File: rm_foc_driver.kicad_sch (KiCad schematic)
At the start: 69 parts, among them J1 SWD, J2 SENSOR, J3 UART, J4 TMC4671, J5 PWM, J6 Conn_01x02, J7 CURRENT_SENSE, J8 Conn_01x03, Q1 IRF7580M, Q2 IRF7580M, Q3 IRF7580M, Q4 IRF7580M, Q5 IRF7580M, Q6 IRF7580M, U1 TPS54540, U2 RT9013, U3 STM32F401CCUx, U4 DRV8303, U5 AS5047D, Y1 Crystal_GND24

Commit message: Not complete yet
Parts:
- removed C1: 10uF, Capacitor_SMD:C_0603_1608Metric, symbol Device:C
- removed C14, C18, C19, C20: 100nF, Capacitor_SMD:C_0603_1608Metric, symbol Device:C
- removed C17: 1uF, Capacitor_SMD:C_0603_1608Metric, symbol Device:C
- removed C21: 2.2nF, Capacitor_SMD:C_0603_1608Metric, symbol Device:C
- removed J7: CURRENT_SENSE, Connector_PinHeader_2.54mm:PinHeader_1x02_P2.54mm_Vertical, symbol Connector_Generic:Conn_01x02
- removed U4: DRV8303, Package_SO:TSSOP-48_6.1x12.5mm_P0.5mm, symbol Driver_Motor:DRV8303
- removed U5: AS5047D, Package_SO:TSSOP-14_4.4x5mm_P0.65mm, symbol Sensor_Magnetic:AS5047D
- added C10: 100nF, Capacitor_SMD:C_0603_1608Metric, symbol Device:C
- added D4, D5, D6: DIODE, Diode_SMD:D_SMA, symbol pspice:DIODE
- added R12: 200k, Resistor_SMD:R_0603_1608Metric, symbol Device:R
- added R13, R14, R15, R16, R17, R18: 10R, Resistor_SMD:R_0603_1608Metric, symbol Device:R
- added U4: EG2133, Package_SO:TSSOP-20_4.4x6.5mm_P0.65mm, symbol Driver_FET:EG2133
- added U6: INA2180, Package_SO:VSSOP-8_3.0x3.0mm_P0.65mm, symbol Amplifier_Current:INA2180
- added U7: MT6701, Package_SO:SOP-8_3.9x4.9mm_P1.27mm, symbol Sensor_Magnetic:MT6701
- C12, C13: value 1uF -> 100nF
- C15: value 2.2uF -> 1uF
- C16: value 4.7uF -> 1uF; footprint Capacitor_SMD:C_0805_2012Metric -> Capacitor_SMD:C_0603_1608Metric
- R9: value 1R -> 200k
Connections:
- net +12V: no longer C16.1
- net +5V: now also C15.1, C16.1, R9.1, D4.1 (K), D5.1 (K), D6.1 (K), R12.2, U4.7 (VCC), U6.8 (VS), U7.1 (VDD)
- net GH_A: now also R13.2
- net GH_B: now also R15.2
- net GH_C: now also R17.2
- net GL_A: now also R14.2
- net GL_B: now also R16.2
- net GL_C: now also R18.2
- net GND: now also C15.2, U4.8 (GND), U6.2 (IN1-), U6.4 (GND), U6.6 (IN2-), U7.4 (GND); no longer C12.2, C13.2, C15.1, R9.2
- net PWM1: now also U4.1 (HIN1)
- net PWM2: now also U4.2 (HIN2)
- net PWM3: now also U4.3 (HIN3)
- net PWM4: now also U4.4 (~{LIN1})
- net PWM5: now also U4.5 (~{LIN2})
- net PWM6: now also U4.6 (~{LIN3})
- net SH_A: now also C10.2, U4.12 (VS1)
- net SH_B: now also C12.2, U4.15 (VS2)
- net SH_C: now also C13.2, U4.18 (VS3)
- net SL_A: now also U6.3 (IN1+)
- net SL_B: now also U6.5 (IN2+)
- net SO1: now also U6.1 (OUT1)
- net SO2: now also U6.7 (OUT2)
- net at C12.1: now also D5.2 (A), U4.17 (VB2)
- net at C13.1: now also D4.2 (A), U4.20 (VB3)
- new net: R14.1, U4.9 (LO1)
- new net: R13.1, U4.13 (HO1)
- new net: R16.1, U4.10 (LO2)
- new net: R18.1, U4.11 (LO3)
- new net: C10.1, D6.2 (A), U4.14 (VB1)
- new net: R15.1, U4.16 (HO2)
- new net: R17.1, U4.19 (HO3)
- new net: R9.2, U7.2 (MODE)
- new net: R12.1, U7.8 (Z)
- no-connect marks 30 -> 25

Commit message: new verson of pcb.ready to print
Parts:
- removed J2: SENSOR, Connector_PinHeader_2.54mm:PinHeader_1x03_P2.54mm_Vertical, symbol Connector_Generic:Conn_01x03
- removed R12, R9: 200k, Resistor_SMD:R_0603_1608Metric, symbol Device:R
- D3, D4, D5, D6: footprint Diode_SMD:D_SMA -> Diode_SMD:D_SOD-123
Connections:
- net CS1: now also U7.8 (Z)
- net CS2: now also J4.4 (Pin_4)
- net MISO: now also U7.6 (A)
- net OSC_IN: now also C9.1, Y1.1; no longer C11.1, Y1.3
- net OSC_OUT: now also C11.1, Y1.3; no longer C9.1, Y1.1
- net SCLK: now also U7.7 (B)
- net ADC1: now reaches U3.18 (PB0)
- net ADC1: now also U7.3 (OUT)
- net MODE: now reaches U3.19 (PB1)
- net MODE: now also U7.2 (MODE)
- net CS3: no longer names the net of U3.29 (PA8)
- net CS3: no longer J4.4 (Pin_4)
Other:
- moved on the sheet: C16, J8, U7

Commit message: Update pcb-layout.Not complete yet.Current progress 50%.
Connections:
- net DC_CAL: no longer names the net of U3.11 (PA1)
- net EN_GATE: no longer names the net of U3.12 (PA2)
- no-connect marks 25 -> 27
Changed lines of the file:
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@@
   (junction (at 217.805 232.41) (diameter 0) (color 0 0 0 0)
   )
+  (no_connect (at 113.665 252.095))
+  (no_connect (at 113.665 254.635))
   (no_connect (at 113.665 249.555))
   (no_connect (at 69.85 46.99))
@@
     (stroke (width 0) (type default) (color 0 0 0 0))
   )
-  (wire (pts (xy 113.665 254.635) (xy 123.825 254.635))
-    (stroke (width 0) (type default) (color 0 0 0 0))
-  )
   (wire (pts (xy 71.755 267.335) (xy 80.645 267.335))
     (stroke (width 0) (type default) (color 0 0 0 0))
@@
   )
   (wire (pts (xy 30.48 340.36) (xy 43.815 340.36))
-    (stroke (width 0) (type default) (color 0 0 0 0))
-  )
-  (wire (pts (xy 113.665 252.095) (xy 123.825 252.095))
     (stroke (width 0) (type default) (color 0 0 0 0))
   )
@@
     (effects (font (size 1.27 1.27)) (justify left bottom))
   )
-  (label "EN_GATE" (at 123.825 254.635 0)
-    (effects (font (size 1.27 1.27)) (justify left bottom))
-  )
   (label "CS2" (at 123.825 259.715 0)
     (effects (font (size 1.27 1.27)) (justify left bottom))
@@
     (effects (font (size 1.27 1.27)) (justify left bottom))
   )
-  (label "DC_CAL" (at 123.825 252.095 0)
-    (effects (font (size 1.27 1.27)) (justify left bottom))
-  )

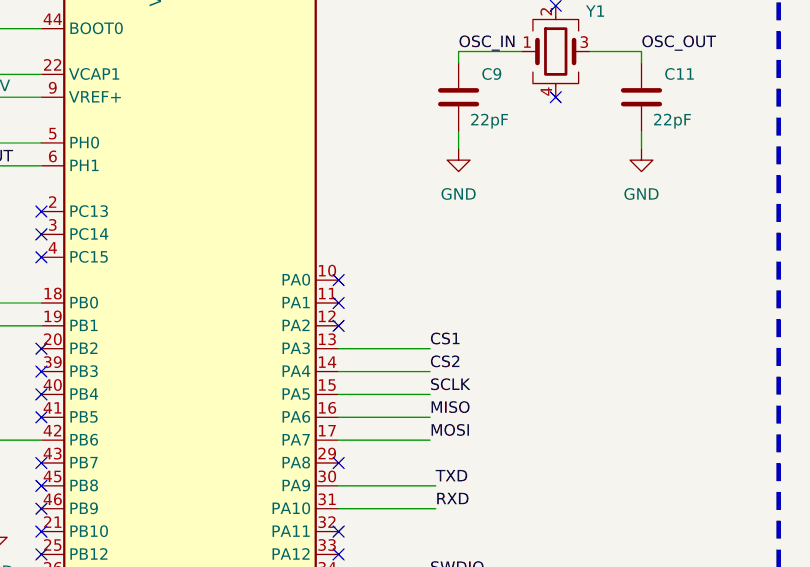
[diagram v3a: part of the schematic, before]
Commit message: Straight line version.
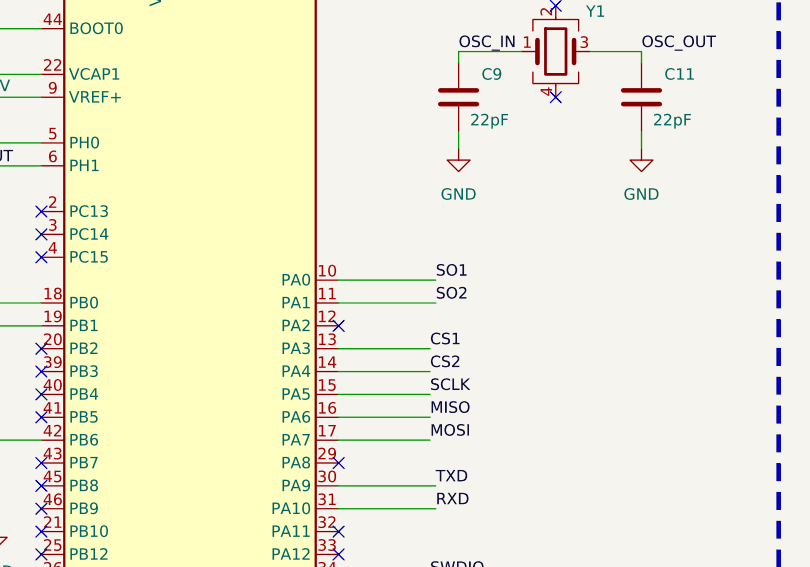
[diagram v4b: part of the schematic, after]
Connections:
- net SO1: now also U3.10 (PA0)
- net SO2: now also U3.11 (PA1)
- no-connect marks 27 -> 25
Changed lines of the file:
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@@
   (junction (at 217.805 232.41) (diameter 0) (color 0 0 0 0)
   )
-  (no_connect (at 113.665 252.095))
   (no_connect (at 113.665 254.635))
-  (no_connect (at 113.665 249.555))
   (no_connect (at 69.85 46.99))
   (no_connect (at 137.795 229.235))
@@
     (stroke (width 0) (type default) (color 0 0 0 0))
   )
+  (wire (pts (xy 113.665 249.555) (xy 124.46 249.555))
+    (stroke (width 0) (type default) (color 0 0 0 0))
+  )
   (wire (pts (xy 113.665 267.335) (xy 123.825 267.335))
     (stroke (width 0) (type default) (color 0 0 0 0))
@@
   )
   (wire (pts (xy 71.755 274.32) (xy 75.565 274.32))
+    (stroke (width 0) (type default) (color 0 0 0 0))
+  )
+  (wire (pts (xy 113.665 252.095) (xy 124.46 252.095))
     (stroke (width 0) (type default) (color 0 0 0 0))
   )
@@
     (effects (font (size 1.27 1.27)) (justify left bottom))
   )
+  (label "SO1" (at 124.46 249.555 0)
+    (effects (font (size 1.27 1.27)) (justify left bottom))
+  )
   (label "SCLK" (at 90.17 342.9 0)
     (effects (font (size 1.27 1.27)) (justify left bottom))
@@
     (effects (font (size 1.27 1.27)) (justify left bottom))
   )
+  (label "SO2" (at 124.46 252.095 0)
+    (effects (font (size 1.27 1.27)) (justify left bottom))
+  )

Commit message: Fcuk IRF7580 fuck fuck.csd18540 is better
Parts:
- removed J5: PWM, Connector_PinHeader_2.54mm:PinHeader_1x06_P2.54mm_Vertical, symbol Connector_Generic:Conn_01x06
- removed Q1, Q2, Q3, Q4, Q5, Q6: IRF7580M, Package_DirectFET:DirectFET_ME, symbol Transistor_FET:IRF7580M
- added J5: Conn_01x07, Connector_PinHeader_2.54mm:PinHeader_1x07_P2.54mm_Vertical, symbol Connector_Generic:Conn_01x07
- added Q1, Q2, Q3, Q4, Q5, Q6: CSD18540Q5B, Package_TO_SOT_SMD:TDSON-8-1, symbol Transistor_FET:CSD18540Q5B
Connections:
- net +12V: now also Q1.5 (D), Q3.5 (D), Q5.5 (D)
- net GH_A: now also Q1.4 (G)
- net GH_B: now also Q3.4 (G)
- net GH_C: now also Q5.4 (G)
- net GL_A: now also Q2.4 (G)
- net GL_B: now also Q4.4 (G)
- net GL_C: now also Q6.4 (G)
- net GND: now also J5.7 (Pin_7), Q6.1 (S), Q6.2 (S), Q6.3 (S)
- net PWM1: now also J5.1 (Pin_1)
- net PWM2: now also J5.2 (Pin_2)
- net PWM3: now also J5.3 (Pin_3)
- net PWM4: now also J5.4 (Pin_4)
- net PWM5: now also J5.5 (Pin_5)
- net PWM6: now also J5.6 (Pin_6)
- net SH_A: now also Q1.1 (S), Q1.2 (S), Q1.3 (S), Q2.5 (D)
- net SH_B: now also Q3.1 (S), Q3.2 (S), Q3.3 (S), Q4.5 (D)
- net SH_C: now also Q5.1 (S), Q5.2 (S), Q5.3 (S), Q6.5 (D)
- net SL_A: now also Q2.1 (S), Q2.2 (S), Q2.3 (S)
- net SL_B: now also Q4.1 (S), Q4.2 (S), Q4.3 (S)

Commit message: ir2104 version
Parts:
- removed J5: Conn_01x07, Connector_PinHeader_2.54mm:PinHeader_1x07_P2.54mm_Vertical, symbol Connector_Generic:Conn_01x07
- removed R17, R18: 10R, Resistor_SMD:R_0603_1608Metric, symbol Device:R
- removed U4: EG2133, Package_SO:TSSOP-20_4.4x6.5mm_P0.65mm, symbol Driver_FET:EG2133
- added C1: 1uF, Capacitor_SMD:C_0603_1608Metric, symbol Device:C
- added C14, C17, C18: 100nF, Capacitor_SMD:C_0603_1608Metric, symbol Device:C
- added J2: TMC4671, Connector_PinHeader_2.54mm:PinHeader_1x04_P2.54mm_Vertical, symbol Connector_Generic:Conn_01x04
- added R12, R9: 20R, Resistor_SMD:R_0603_1608Metric, symbol Device:R
- added U10: 74HC244, Package_SO:TSSOP-20_4.4x5mm_P0.5mm, symbol 74xx:74HC244
- added U4: AMS1117-5.0, Package_TO_SOT_SMD:SOT-223-3_TabPin2, symbol Regulator_Linear:AMS1117-5.0
- added U5, U8, U9: IR2104, Package_SO:SOIC-8W_5.3x5.3mm_P1.27mm, symbol Driver_FET:IR2104
- R13, R14, R15, R16: value 10R -> 20R
- R7: value 105k -> 210k
- R8: value 20k -> 15k
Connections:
- net +12V: now also C10.1, C12.1, C13.1, D4.1 (K), D5.1 (K), D6.1 (K), L1.2, R7.1, C1.1, U4.3 (VI), U5.1 (VCC), U5.3 (~{SD}), U8.1 (VCC), U8.3 (~{SD}), U9.1 (VCC), U9.3 (~{SD}); no longer C22.1, C24.1, C25.1, C26.1, C27.1, C29.1, C3.1, C30.1, C31.1, C32.1, C33.1, J6.2 (Pin_2), Q1.5 (D), Q3.5 (D), Q5.5 (D), U1.2 (VIN)
- net +5V: now also U10.20 (VCC), U4.2 (VO); no longer D4.1 (K), D5.1 (K), D6.1 (K), L1.2, R7.1
- net GH_A: now also R13.1; no longer R13.2
- net GH_B: now also R9.1; no longer R15.2
- net GH_C: now also R15.1
- net GL_A: now also R14.1; no longer R14.2
- net GL_B: now also R12.1; no longer R16.2
- net GL_C: now also R16.1
- net GND: now also C10.2, C12.2, C13.2, C1.2, J2.4 (Pin_4), U10.1 (1OE), U10.10 (GND), U4.1 (GND), U5.4 (COM), U8.4 (COM), U9.4 (COM)
- net PWM1: now also J2.1 (Pin_1), U10.2 (1A0)
- net PWM2: now also J2.2 (Pin_2), U10.4 (1A1)
- net PWM3: now also J2.3 (Pin_3), U10.6 (1A2)
- net SH_A: now also C17.2, U8.6 (VS); no longer C10.2
- net SH_B: now also C14.2, U5.6 (VS); no longer C12.2
- net SH_C: now also C18.2, U9.6 (VS); no longer C13.2
- net at D4.2 (A): now also C14.1, U5.8 (VB); no longer C13.1
- net at D5.2 (A): now also C17.1, U8.8 (VB); no longer C12.1
- net at D6.2 (A): now also C18.1, U9.8 (VB); no longer C10.1
- new net: R16.2, U9.5 (LO)
- new net: R15.2, U9.7 (HO)
- new net: R14.2, U8.5 (LO)
- new net: R13.2, U8.7 (HO)
- new net: R12.2, U5.5 (LO)
- new net: R9.2, U5.7 (HO)
- new net +24V: C22.1, C24.1, C25.1, C26.1, C27.1, C29.1, C3.1, C30.1, C31.1, C32.1, C33.1, J6.2 (Pin_2), Q1.5 (D), Q3.5 (D), Q5.5 (D), U1.2 (VIN)
- new net PWMA: U10.18 (1Y0), U9.2 (IN)
- new net PWMB: U10.16 (1Y1), U5.2 (IN)
- new net PWMC: U10.14 (1Y2), U8.2 (IN)
- no-connect marks 25 -> 36
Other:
- note added: "BUCK TO 12V"
- note added: "CURRENT SENSE"
- note added: "Chen Yulong"
- note added: "DynamicX"
- note added: "ISOLATE"
- note added: "POSITION SENSOR"
- note removed: "SENSOR"
- company: (none) -> Chen Yulong
- title: (none) -> DynamicX FOC_Driver
- moved on the sheet: C11, C15, C2, C22, C24, C25, C26, C27, C29, C30, C31, C32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

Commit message: update package
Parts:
- U10: footprint Package_SO:TSSOP-20_4.4x5mm_P0.5mm -> Package_SO:TSSOP-20_4.4x6.5mm_P0.65mm
- U5, U8, U9: footprint Package_SO:SOIC-8W_5.3x5.3mm_P1.27mm -> Package_SO:SOP-8_3.9x4.9mm_P1.27mm
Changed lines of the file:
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@@
     (stroke (width 0) (type default) (color 0 0 0 0))
   )
-  (wire (pts (xy 193.04 281.94) (xy 193.04 297.18))
+  (wire (pts (xy 193.04 281.94) (xy 193.04 290.195))
     (stroke (width 0) (type default) (color 0 0 0 0))
   )
@@
       (effects (font (size 1.27 1.27)) (justify left))
     )
-    (property "Footprint" "Package_SO:SOIC-8W_5.3x5.3mm_P1.27mm" (id 2) (at 213.36 57.15 0)
-      (effects (font (size 1.27 1.27) italic) hide)
+    (property "Footprint" "Package_SO:SOP-8_3.9x4.9mm_P1.27mm" (id 2) (at 213.36 57.15 0)
+      (effects (font (size 1.27 1.27) italic))
     )
     (property "Datasheet" "https://www.infineon.com/dgdl/ir2104.pdf?fileId=5546d462533600a4015355c7c1c31671" (id 3) (at 213.36 57.15 0)
@@
       (effects (font (size 1.27 1.27)) (justify left))
     )
-    (property "Footprint" "Package_SO:TSSOP-20_4.4x5mm_P0.5mm" (id 2) (at 388.112 340.741 0)
+    (property "Footprint" "Package_SO:TSSOP-20_4.4x6.5mm_P0.65mm" (id 2) (at 388.112 340.741 0)
       (effects (font (size 1.27 1.27)) hide)
     )
@@
     (pin "1")
   )
-  (symbol (lib_id "power:GND") (at 193.04 297.18 0) (unit 1)
+  (symbol (lib_id "power:GND") (at 193.04 290.195 0) (unit 1)
     (in_bom yes) (on_board yes) (fields_autoplaced)
-    (property "Reference" "#PWR0112" (id 0) (at 193.04 303.53 0)
+    (property "Reference" "#PWR0112" (id 0) (at 193.04 296.545 0)
       (effects (font (size 1.27 1.27)) hide)
     )
-    (property "Value" "GND" (id 1) (at 193.04 302.26 0))
-    (property "Footprint" "" (id 2) (at 193.04 297.18 0)
+    (property "Value" "GND" (id 1) (at 193.04 295.275 0))
+    (property "Footprint" "" (id 2) (at 193.04 290.195 0)
       (effects (font (size 1.27 1.27)) hide)
     )
-    (property "Datasheet" "" (id 3) (at 193.04 297.18 0)
+    (property "Datasheet" "" (id 3) (at 193.04 290.195 0)
       (effects (font (size 1.27 1.27)) hide)
     )
@@
       (effects (font (size 1.27 1.27)) (justify left))
     )
-    (property "Footprint" "Package_SO:SOIC-8W_5.3x5.3mm_P1.27mm" (id 2) (at 212.09 189.23 0)
+    (property "Footprint" "Package_SO:SOP-8_3.9x4.9mm_P1.27mm" (id 2) (at 212.09 189.23 0)
       (effects (font (size 1.27 1.27) italic) hide)
     )
@@
       (effects (font (size 1.27 1.27)) (justify left))
     )
-    (property "Footprint" "Package_SO:SOIC-8W_5.3x5.3mm_P1.27mm" (id 2) (at 212.09 125.73 0)
+    (property "Footprint" "Package_SO:SOP-8_3.9x4.9mm_P1.27mm" (id 2) (at 212.09 125.73 0)
       (effects (font (size 1.27 1.27) italic) hide)
     )
@@
     )
     (path "/d8267b9d-7a7c-4f47-9f71-e9dc0f2800b7"
-      (reference "U5") (unit 1) (value "IR2104") (footprint "Package_SO:SOIC-8W_5.3x5.3mm_P1.27mm")
+      (reference "U5") (unit 1) (value "IR2104") (footprint "Package_SO:SOP-8_3.9x4.9mm_P1.27mm")
     )
     (path "/0a77004e-a8ec-450b-8d29-c6a707b2ba5d"
@@
     )
     (path "/c6946031-3d0c-4e1b-a27b-45834de6dc09"
-      (reference "U8") (unit 1) (value "IR2104") (footprint "Package_SO:SOIC-8W_5.3x5.3mm_P1.27mm")
+      (reference "U8") (unit 1) (value "IR2104") (footprint "Package_SO:SOP-8_3.9x4.9mm_P1.27mm")
     )
     (path "/00bf1c12-25f3-439d-a9dd-699c6c179296"
-      (reference "U9") (unit 1) (value "IR2104") (footprint "Package_SO:SOIC-8W_5.3x5.3mm_P1.27mm")
+      (reference "U9") (unit 1) (value "IR2104") (footprint "Package_SO:SOP-8_3.9x4.9mm_P1.27mm")
     )
     (path "/7022984f-8822-4353-a698-f2aa82d9fb23"
-      (reference "U10") (unit 1) (value "74HC244") (footprint "Package_SO:TSSOP-20_4.4x5mm_P0.5mm")
+      (reference "U10") (unit 1) (value "74HC244") (footprint "Package_SO:TSSOP-20_4.4x6.5mm_P0.65mm")
     )
     (path "/d494d9af-80f2-455e-a88b-09ded4b856c8"

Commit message: version 1.1.0-beta
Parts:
- removed U4: AMS1117-5.0, Package_TO_SOT_SMD:SOT-223-3_TabPin2, symbol Regulator_Linear:AMS1117-5.0
- added C19, C23: 47uF, Capacitor_SMD:C_0805_2012Metric, symbol Device:C
- added C20, C21: 1uF, Capacitor_SMD:C_0603_1608Metric, symbol Device:C
- added J5: Conn_01x03, Connector_PinSocket_2.54mm:PinSocket_1x03_P2.54mm_Vertical, symbol Connector_Generic:Conn_01x03
- added L2: 2.2uH, Inductor_SMD:L_Neosid_Ms42, symbol pspice:INDUCTOR
- added R17: 190k, Resistor_SMD:R_0603_1608Metric, symbol Device:R
- added R18, R19: 10k, Resistor_SMD:R_0603_1608Metric, symbol Device:R
- added R20: 105k, Resistor_SMD:R_0603_1608Metric, symbol Device:R
- added U4: SY8303, Package_TO_SOT_SMD:TSOT-23-8, symbol Converter_DCDC:SY8303
- C1: value 1uF -> 10nF
- L1: footprint Inductor_SMD:L_7.3x7.3_H4.5 -> Inductor_SMD:L_Neosid_Ms42
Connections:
- net CS2 is gone; now on net CS1: J4.4 (Pin_4), U3.14 (PA4)
- net +12V: now also C19.1, R20.1, U4.5 (IN); no longer C1.1
- net +3.3V: now also C20.1
- net +5V: now also U7.2 (MODE), C21.1, C23.1, L2.1, R17.1
- net ADC1: no longer U7.3 (OUT)
- net GND: now also C19.2, C20.2, C21.2, C23.2, J5.3 (Pin_3), R18.2, R19.2, U4.3 (GND), U4.4 (GND); no longer C1.2
- net MODE: no longer U7.2 (MODE)
- net SH_A: now also J8.1 (Pin_1); no longer J8.3 (Pin_3)
- net SH_C: now also J8.3 (Pin_3); no longer J8.1 (Pin_1)
- net SO1: now also J5.1 (Pin_1)
- net SO2: now also J5.2 (Pin_2)
- new net: R20.2, U4.8 (EN)
- new net: C1.2, L2.2, U4.6 (LX)
- new net: R17.2, R18.1, U4.1 (FB)
- new net: R19.1, U4.2 (FS)
- new net: C1.1, U4.7 (BS)
- no-connect marks 36 -> 37
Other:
- note added: "3.3V LDO"
- note added: "L=[Vout(1-Vout/Vinmax)]/[Fsw*Iout*0.4]"
- note added: "Vout=0.6*(1+R1/R2)"
- note removed: "BUCK TO 3.3V"
- moved on the sheet: C15, U10
